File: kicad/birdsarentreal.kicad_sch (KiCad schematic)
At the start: 31 parts, among them J1 Adafruit Coil Jumper, J2 Adafruit Coil Jumper, J3 Adafruit Coil Jumper, J4 Adafruit Coil Jumper, Q2 NMOS, U9 MCP73831-2-OT

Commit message: First PCB Layout complete
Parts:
- removed S3: TM1000Q, TM1000Q:SW_TM1000Q, symbol TM1000Q:TM1000Q
- added D1: D, Diode_SMD:D_0805_2012Metric_Pad1.15x1.40mm_HandSolder, symbol Device:D
- added R1: 2k, Resistor_SMD:R_0805_2012Metric_Pad1.20x1.40mm_HandSolder, symbol Device:R
- added S2: TM1000Q, TM1000Q:SW_TM1000Q, symbol TM1000Q:TM1000Q
- added TP1: TestPoint, TestPoint:TestPoint_Pad_D2.0mm, symbol Connector:TestPoint
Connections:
- net Controller/GND: now also Q2.1 (D)
- net Controller/MOSTRIG: now also D1.2 (A); no longer Q2.2 (G)
- net Controller/VBAT: now also S2.2
- net at BT2.2 (-), C10.2, J1.2 (Pin_2)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: now also Q2.3 (S), R1.2; no longer Q2.1 (D)
- new net: D1.1 (K), Q2.2 (G), R1.1, S2.1, S2.3, TP1.1
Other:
- moved on the sheet: AP7366EA1, C11, C12, F2, J1, J4, Q2, TP1

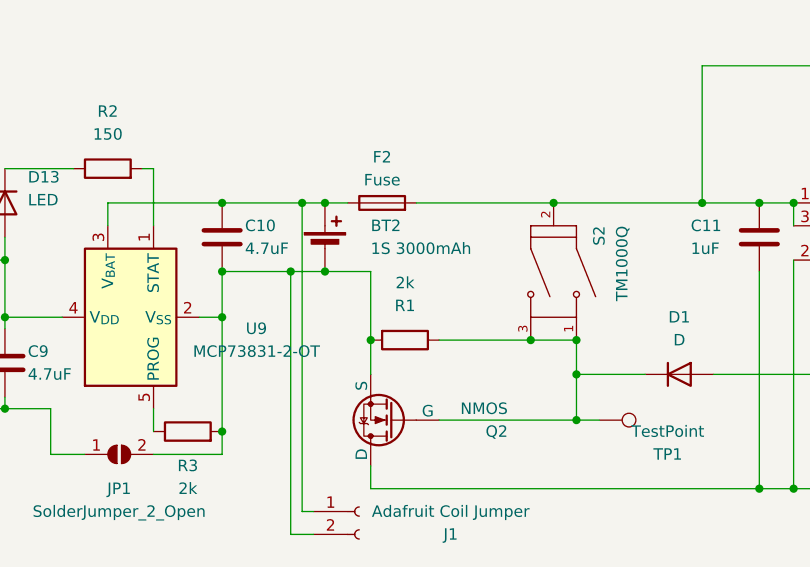
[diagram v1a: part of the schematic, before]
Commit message: Fix banned pins on ESP32
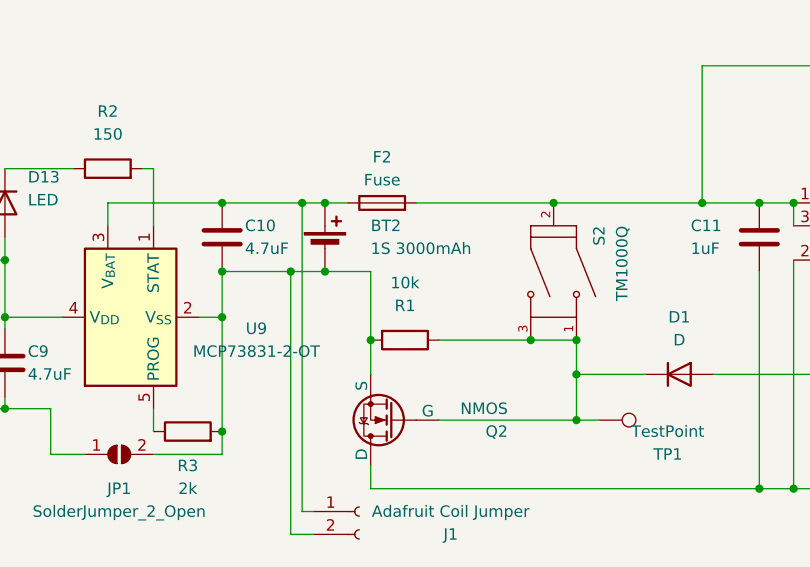
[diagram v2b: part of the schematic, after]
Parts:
- R1: value 2k -> 10k
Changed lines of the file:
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@@
       (effects (font (size 1.27 1.27)))
     )
-    (property "Value" "2k" (at 138.43 87.63 90)
+    (property "Value" "10k" (at 138.43 87.63 90)
       (effects (font (size 1.27 1.27)))
     )

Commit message: Make schematic pretty
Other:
- note added: "3.3V LDO"
- note added: "5V LDO"
- note added: "BMS"
- note added: "ESP32 CIRCUITRY"
- note added: "ESP32 I/O"
- note added: "ON/OFF CIRCUIT"
- note added: "Resonant Inductive Receiver and Doubled Full-Bridge Rectifier"
- note added: "TILT SWITCH"
- note added: "TURNS ON WHEN ROBOT TURNED PAST 45 DEG FROM HORIZONTAL OR IF ESP32 COMMANDS"
- moved on the sheet: AP7366EA1, BT2, C10, C11, C12, C9, D1, D13, F2, J1, J4, JP1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

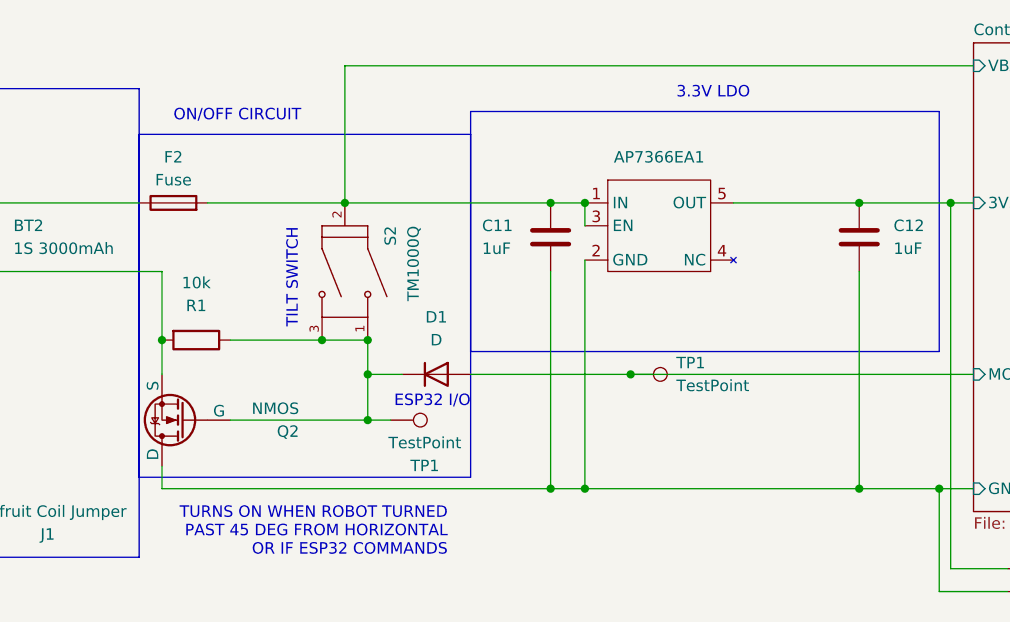
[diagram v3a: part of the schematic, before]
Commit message: Fix MOSFET footprint pinout
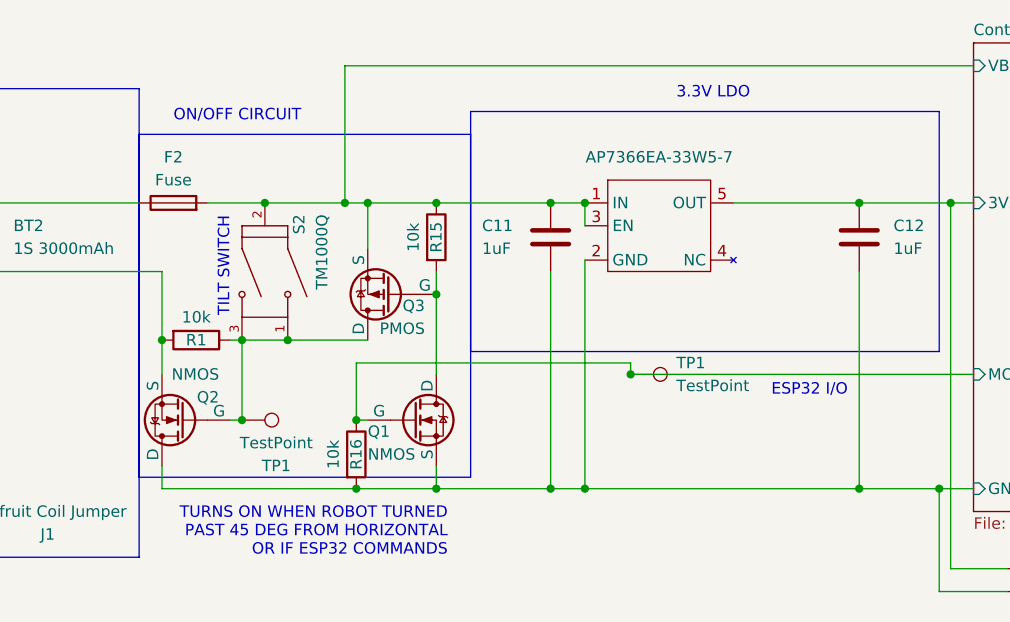
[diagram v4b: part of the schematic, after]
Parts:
- removed D1: D, Diode_SMD:D_0805_2012Metric_Pad1.15x1.40mm_HandSolder, symbol Device:D
- added Q1: NMOS, Package_TO_SOT_SMD:SOT-323_SC-70_Handsoldering, symbol Simulation_SPICE:NMOS
- added Q3: PMOS, Package_TO_SOT_SMD:SOT-323_SC-70_Handsoldering, symbol Simulation_SPICE:PMOS
- added R15, R16: 10k, Resistor_SMD:R_0805_2012Metric_Pad1.20x1.40mm_HandSolder, symbol Device:R
- renumbered AP7366EA1 to AP7366EA-33W5-7
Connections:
- net Controller/GND: now also Q2.3 (D), Q1.2 (S), R16.2; no longer Q2.1 (D)
- net Controller/MOSTRIG: now also Q1.1 (G), R16.1
- net Controller/VBAT: now also Q3.2 (S), R15.1
- net at BT2.2 (-), C10.2, J1.2 (Pin_2)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: now also Q2.2 (S); no longer Q2.3 (S)
- net at R1.1, S2.1, S2.3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: now also Q2.1 (G), Q3.3 (D); no longer Q2.2 (G)
- new net: Q1.3 (D), Q3.1 (G), R15.2
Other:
- moved on the sheet: S2, TP1

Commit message: Change battery connector
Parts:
- BT2: footprint Connector_JST:JST_GH_BM02B-GHS-TBT_1x02-1MP_P1.25mm_Vertical -> Connector_JST:JST_XH_B2B-XH-A_1x02_P2.50mm_Vertical
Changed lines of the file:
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@@
       (effects (font (size 1.27 1.27)) hide)
     )
-    (pin "3")
     (pin "1")
     (pin "2")
+    (pin "3")
     (instances
       (project "robot"
@@
       (effects (font (size 1.27 1.27)) (justify left))
     )
-    (property "Footprint" "Connector_JST:JST_GH_BM02B-GHS-TBT_1x02-1MP_P1.25mm_Vertical" (at 138.43 82.296 90)
+    (property "Footprint" "Connector_JST:JST_XH_B2B-XH-A_1x02_P2.50mm_Vertical" (at 138.43 82.296 90)
       (effects (font (size 1.27 1.27)) hide)
     )
@@
       (effects (font (size 1.27 1.27)) hide)
     )
-    (pin "3")
     (pin "1")
     (pin "2")
+    (pin "3")
     (instances
       (project "robot"

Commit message: Final PCB
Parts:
- AP7366EA-33W5-7: value ~ -> AP7366EA-33W5-7
- D10, D11, D12, D9: value D -> SD0805S020S1R0
- D13: value LED -> LTST-C171GKT
- F1: value Fuse -> MFU0805FF01000P100
- F2: value Fuse -> MFU0805FF03000P100
- Q1, Q2: value NMOS -> DMG1012UW-7
- Q3: value PMOS -> DMG1013UW-7
- U7: value ~ -> R1500H050B1
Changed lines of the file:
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@@
   (symbol (lib_id "Device:Fuse") (at 160.02 78.74 90) (unit 1)
     (in_bom yes) (on_board yes) (dnp no) (fields_autoplaced)
-    (property "Reference" "F2" (at 160.02 73.66 90)
-      (effects (font (size 1.27 1.27)))
-    )
-    (property "Value" "Fuse" (at 160.02 76.2 90)
-      (effects (font (size 1.27 1.27)))
+    (property "Reference" "F2" (at 160.02 76.2 90)
+      (effects (font (size 1.27 1.27)))
+    )
+    (property "Value" "MFU0805FF03000P100" (at 160.02 76.2 90)
+      (effects (font (size 1.27 1.27)) hide)
     )
     (property "Footprint" "Fuse:Fuse_0805_2012Metric_Pad1.15x1.40mm_HandSolder" (at 160.02 80.518 90)
@@
       (effects (font (size 1.27 1.27)) (justify left))
     )
-    (property "Value" "LED" (at 99.06 78.4225 90)
-      (effects (font (size 1.27 1.27)) (justify left))
+    (property "Value" "LTST-C171GKT\n" (at 99.06 78.4225 90)
+      (effects (font (size 1.27 1.27)) (justify left) hide)
     )
     (property "Footprint" "LED_SMD:LED_0805_2012Metric_Pad1.15x1.40mm_HandSolder" (at 96.52 78.74 0)
@@
       (effects (font (size 1.27 1.27)) (justify left))
     )
-    (property "Value" "NMOS" (at 181.61 106.68 0)
-      (effects (font (size 1.27 1.27)) (justify left))
+    (property "Value" "DMG1012UW-7" (at 181.61 106.68 0)
+      (effects (font (size 1.27 1.27)) (justify left) hide)
     )
     (property "Footprint" "Package_TO_SOT_SMD:SOT-323_SC-70_Handsoldering" (at 191.77 100.33 0)
@@
   (symbol (lib_id "Device:Fuse") (at 54.61 85.09 90) (unit 1)
     (in_bom yes) (on_board yes) (dnp no) (fields_autoplaced)
-    (property "Reference" "F1" (at 54.61 80.01 90)
-      (effects (font (size 1.27 1.27)))
-    )
-    (property "Value" "Fuse" (at 54.61 82.55 90)
-      (effects (font (size 1.27 1.27)))
+    (property "Reference" "F1" (at 54.61 82.55 90)
+      (effects (font (size 1.27 1.27)))
+    )
+    (property "Value" "MFU0805FF01000P100\n" (at 54.61 82.55 90)
+      (effects (font (size 1.27 1.27)) hide)
     )
     (property "Footprint" "Fuse:Fuse_0805_2012Metric_Pad1.15x1.40mm_HandSolder" (at 54.61 86.868 90)
@@
       (effects (font (size 1.27 1.27)))
     )
-    (property "Value" "D" (at 36.83 99.06 0)
-      (effects (font (size 1.27 1.27)))
+    (property "Value" "SD0805S020S1R0\n" (at 36.83 99.06 0)
+      (effects (font (size 1.27 1.27)) hide)
     )
     (property "Footprint" "Diode_SMD:D_0805_2012Metric_Pad1.15x1.40mm_HandSolder" (at 36.83 92.71 0)
@@
       (effects (font (size 1.27 1.27)))
     )
-    (property "Value" "~" (at 214.63 81.28 0)
-      (effects (font (size 1.27 1.27)))
+    (property "Value" "AP7366EA-33W5-7" (at 214.63 81.28 0)
+      (effects (font (size 1.27 1.27)) hide)
     )
     (property "Footprint" "Package_TO_SOT_SMD:SOT-23-5_HandSoldering" (at 214.63 81.28 0)
@@
       (effects (font (size 1.27 1.27)) (justify left))
     )
-    (property "Value" "PMOS" (at 187.96 92.71 0)
-      (effects (font (size 1.27 1.27)) (justify left))
+    (property "Value" "DMG1013UW-7" (at 187.96 92.71 0)
+      (effects (font (size 1.27 1.27)) (justify left) hide)
     )
     (property "Footprint" "Package_TO_SOT_SMD:SOT-323_SC-70_Handsoldering" (at 179.07 91.44 0)
@@
       (effects (font (size 1.27 1.27)) (justify left))
     )
-    (property "Value" "D" (at 43.18 90.17 90)
-      (effects (font (size 1.27 1.27)) (justify left))
+    (property "Value" "SD0805S020S1R0\n" (at 43.18 90.17 90)
+      (effects (font (size 1.27 1.27)) (justify left) hide)
     )
     (property "Footprint" "Diode_SMD:D_0805_2012Metric_Pad1.15x1.40mm_HandSolder" (at 40.64 88.9 0)
@@
       (effects (font (size 1.27 1.27)) (justify left))
     )
-    (property "Value" "NMOS" (at 165.1 97.79 0)
-      (effects (font (size 1.27 1.27)) (justify left))
+    (property "Value" "DMG1012UW-7" (at 165.1 97.79 0)
+      (effects (font (size 1.27 1.27)) (justify left) hide)
     )
     (property "Footprint" "Package_TO_SOT_SMD:SOT-323_SC-70_Handsoldering" (at 156.21 105.41 0)
@@
       (effects (font (size 1.27 1.27)) (justify right))
     )
-    (property "Value" "~" (at 67.31 86.36 0)
-      (effects (font (size 1.27 1.27)))
+    (property "Value" "R1500H050B1" (at 67.31 86.36 0)
+      (effects (font (size 1.27 1.27)) hide)
     )
     (property "Footprint" "Package_TO_SOT_SMD:SOT-89-5" (at 67.31 86.36 0)
@@
       (effects (font (size 1.27 1.27)))
     )
-    (property "Value" "D" (at 36.83 81.28 0)
-      (effects (font (size 1.27 1.27)))
+    (property "Value" "SD0805S020S1R0" (at 36.83 81.28 0)
+      (effects (font (size 1.27 1.27)) hide)
     )
     (property "Footprint" "Diode_SMD:D_0805_2012Metric_Pad1.15x1.40mm_HandSolder" (at 36.83 85.09 0)
@@
   )
   (symbol (lib_id "Device:D") (at 33.02 88.9 270) (unit 1)
-    (in_bom yes) (on_board yes) (dnp no) (fields_autoplaced)
+    (in_bom yes) (on_board yes) (dnp no)
     (property "Reference" "D9" (at 35.56 87.63 90)
       (effects (font (size 1.27 1.27)) (justify left))
     )
-    (property "Value" "D" (at 35.56 90.17 90)
-      (effects (font (size 1.27 1.27)) (justify left))
+    (property "Value" "SD0805S020S1R0\n" (at 34.29 88.9 90)
+      (effects (font (size 1.27 1.27)) (justify left) hide)
     )
     (property "Footprint" "Diode_SMD:D_0805_2012Metric_Pad1.15x1.40mm_HandSolder" (at 33.02 88.9 0)
